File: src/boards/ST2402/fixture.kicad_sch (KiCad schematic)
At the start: 24 parts, among them J11 Conn_02x02_Top_Bottom, J12 Conn_02x02_Top_Bottom, J13 BNC, J14 Screw_Terminal_01x01, J18 Screw_Terminal_01x01, J19 BNC, J21 Conn_02x03_Top_Bottom, J22 Conn_02x03_Top_Bottom

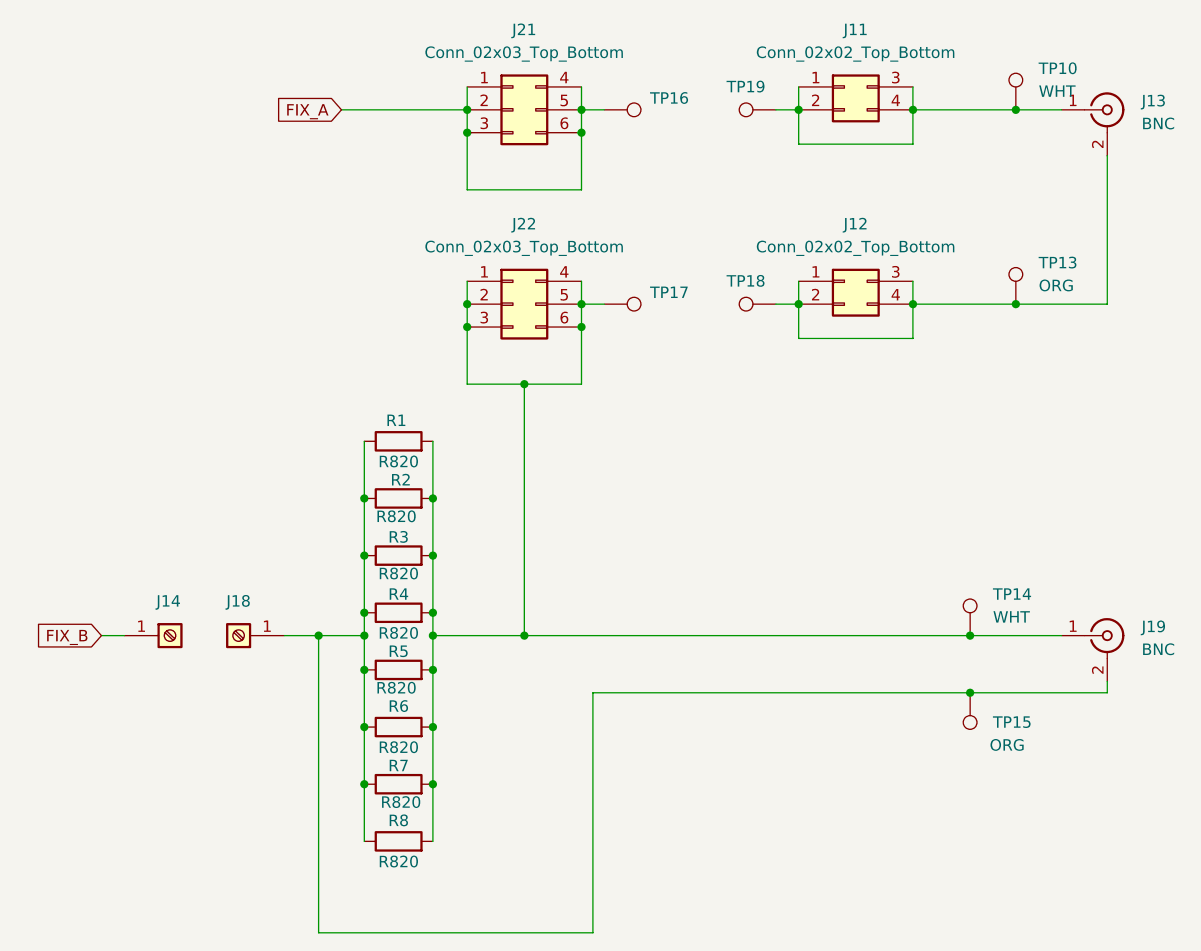
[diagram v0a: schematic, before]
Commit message: Updated pcb files
Added r2 and r3 gerbers and updated KiCad file (r3)
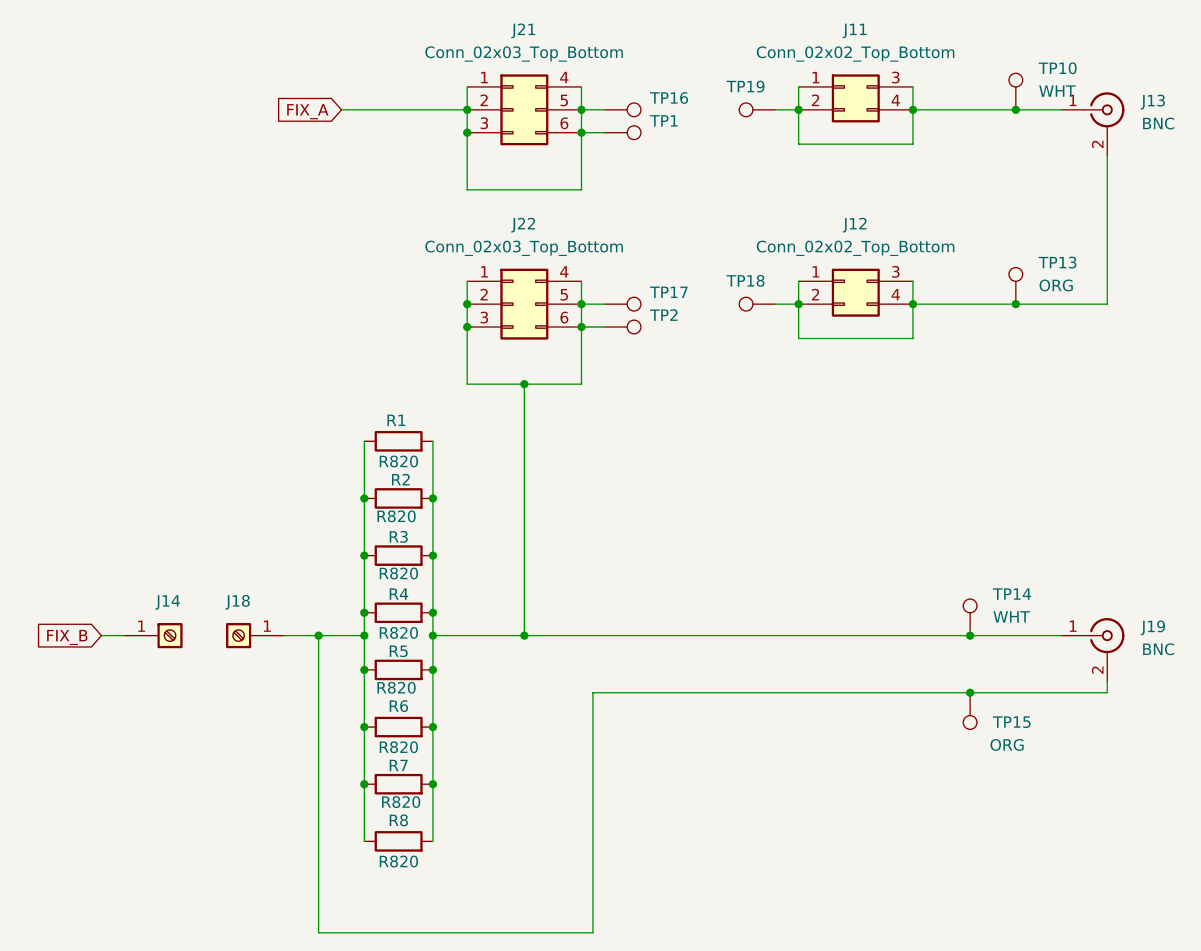
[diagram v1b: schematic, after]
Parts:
- added TP1, TP2: TestPoint, TestPoint:TestPoint_Plated_Hole_D5.0mm, symbol Connector:TestPoint
- J13, J19: footprint Connector_Coaxial:BNC_Amphenol_B6252HB-NPP3G-50_Horizontal -> Connector_Coaxial:BNC_TEConnectivity_1478204_Vertical
- R1, R2, R3, R4, R5, R6, R7, R8: footprint Resistor_SMD:R_0805_2012Metric -> Resistor_SMD:R_1206_3216Metric
- TP10, TP13, TP14, TP15: footprint TestPoint:TestPoint_THTPad_D2.0mm_Drill1.0mm -> TestPoint:TestPoint_Keystone_5010-5014_Multipurpose
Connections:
- net FIX_A: now also TP1.1
- net at J19.1 (In), J22.1 (Pin_1), J22.2 (Pin_2)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: now also TP2.1
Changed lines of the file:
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@@
 (kicad_sch
-	(version 20231120)
+	(version 20250114)
 	(generator "eeschema")
-	(generator_version "8.0")
+	(generator_version "9.0")
 	(paper "USLetter")
 	(title_block
@@
 	(wire
 		(pts
+			(xy 124.46 58.42) (xy 127 58.42)
+		)
+		(stroke
+			(width 0)
+			(type default)
+		)
+	)
+	(wire
+		(pts
 			(xy 161.29 55.88) (xy 161.29 59.69)
 		)
@@
 		(pts
 			(xy 161.29 53.34) (xy 161.29 55.88)
+		)
+		(stroke
+			(width 0)
+			(type default)
+		)
+	)
+	(wire
+		(pts
+			(xy 124.46 80.01) (xy 127 80.01)
 		)
 		(stroke
@@
 			)
 		)
-		(property "Footprint" "TestPoint:TestPoint_THTPad_D2.0mm_Drill1.0mm"
+		(property "Footprint" "TestPoint:TestPoint_Keystone_5010-5014_Multipurpose"
 			(at 177.8 55.88 0)
 			(effects
@@
 			)
 		)
-		(property "Footprint" "Resistor_SMD:R_0805_2012Metric"
+		(property "Footprint" "Resistor_SMD:R_1206_3216Metric"
 			(at 104.14 113.538 90)
 			(effects
@@
 			)
 		)
-		(property "Footprint" "Resistor_SMD:R_0805_2012Metric"
+		(property "Footprint" "Resistor_SMD:R_1206_3216Metric"
 			(at 104.14 126.238 90)
 			(effects
@@
 			)
 		)
-		(property "Footprint" "TestPoint:TestPoint_THTPad_D2.0mm_Drill1.0mm"
+		(property "Footprint" "TestPoint:TestPoint_Keystone_5010-5014_Multipurpose"
 			(at 172.72 114.3 0)
 			(effects
@@
 			)
 		)
-		(property "Footprint" "Connector_Coaxial:BNC_Amphenol_B6252HB-NPP3G-50_Horizontal"
+		(property "Footprint" "Connector_Coaxial:BNC_TEConnectivity_1478204_Vertical"
 			(at 182.88 55.88 0)
 			(effects
@@
 			)
 		)
-		(property "Footprint" "Resistor_SMD:R_0805_2012Metric"
+		(property "Footprint" "Resistor_SMD:R_1206_3216Metric"
 			(at 104.14 94.488 90)
 			(effects
@@
 				(path "/05d99ba5-bbac-4bd6-931a-0f6166a2e0ac/5d4490ae-cd76-4641-b1a2-87213113c349"
 					(reference "R1")
+					(unit 1)
+				)
+			)
+		)
+	)
+	(symbol
+		(lib_id "Connector:TestPoint")
+		(at 127 58.42 270)
+		(unit 1)
+		(exclude_from_sim no)
+		(in_bom yes)
+		(on_board yes)
+		(dnp no)
+		(fields_autoplaced yes)
+		(property "Reference" "TP1"
+			(at 132.08 57.1499 90)
+			(effects
+				(font
+					(size 1.27 1.27)
+				)
+				(justify left)
+			)
+		)
+		(property "Value" "TestPoint"
+			(at 132.08 59.6899 90)
+			(effects
+				(font
+					(size 1.27 1.27)
+				)
+				(justify left)
+				(hide yes)
+			)
+		)
+		(property "Footprint" "TestPoint:TestPoint_Plated_Hole_D5.0mm"
+			(at 127 63.5 0)
+			(effects
+				(font
+					(size 1.27 1.27)
+				)
+				(hide yes)
+			)
+		)
+		(property "Datasheet" "~"
+			(at 127 63.5 0)
+			(effects
+				(font
+					(size 1.27 1.27)
+				)
+				(hide yes)
+			)
+		)
+		(property "Description" "test point"
+			(at 127 58.42 0)
+			(effects
+				(font
+					(size 1.27 1.27)
+				)
+				(hide yes)
+			)
+		)
+		(pin "1"
+		)
+		(instances
+			(project "ST2402"
+				(path "/05d99ba5-bbac-4bd6-931a-0f6166a2e0ac/5d4490ae-cd76-4641-b1a2-87213113c349"
+					(reference "TP1")
+					(unit 1)
+				)
+			)
+		)
+	)
+	(symbol
+		(lib_id "Connector:TestPoint")
+		(at 127 80.01 270)
+		(unit 1)
+		(exclude_from_sim no)
+		(in_bom yes)
+		(on_board yes)
+		(dnp no)
+		(fields_autoplaced yes)
+		(property "Reference" "TP2"
+			(at 132.08 78.7399 90)
+			(effects
+				(font
+					(size 1.27 1.27)
+				)
+				(justify left)
+			)
+		)
+		(property "Value" "TestPoint"
+			(at 132.08 81.2799 90)
+			(effects
+				(font
+					(size 1.27 1.27)
+				)
+				(justify left)
+				(hide yes)
+			)
+		)
+		(property "Footprint" "TestPoint:TestPoint_Plated_Hole_D5.0mm"
+			(at 127 85.09 0)
+			(effects
+				(font
+					(size 1.27 1.27)
+				)
+				(hide yes)
+			)
+		)
+		(property "Datasheet" "~"
+			(at 127 85.09 0)
+			(effects
+				(font
+					(size 1.27 1.27)
+				)
+				(hide yes)
+			)
+		)
+		(property "Description" "test point"
+			(at 127 80.01 0)
+			(effects
+				(font
+					(size 1.27 1.27)
+				)
+				(hide yes)
+			)
+		)
+		(pin "1"
+		)
+		(instances
+			(project "ST2402"
+				(path "/05d99ba5-bbac-4bd6-931a-0f6166a2e0ac/5d4490ae-cd76-4641-b1a2-87213113c349"
+					(reference "TP2")
 					(unit 1)
 				)
@@
 			)
 		)
-		(property "Footprint" "Resistor_SMD:R_0805_2012Metric"
+		(property "Footprint" "Resistor_SMD:R_1206_3216Metric"
 			(at 104.14 119.888 90)
 			(effects
@@
 			)
 		)
-		(property "Footprint" "Resistor_SMD:R_0805_2012Metric"
+		(property "Footprint" "Resistor_SMD:R_1206_3216Metric"
 			(at 104.14 100.838 90)
 			(effects
@@
 			)
 		)
-		(property "Footprint" "Resistor_SMD:R_0805_2012Metric"
+		(property "Footprint" "Resistor_SMD:R_1206_3216Metric"
 			(at 104.14 132.588 90)
 			(effects
@@
 			)
 		)
-		(property "Footprint" "Connector_Coaxial:BNC_Amphenol_B6252HB-NPP3G-50_Horizontal"
+		(property "Footprint" "Connector_Coaxial:BNC_TEConnectivity_1478204_Vertical"
 			(at 182.88 114.3 0)
 			(effects
@@
 			)
 		)
-		(property "Footprint" "TestPoint:TestPoint_THTPad_D2.0mm_Drill1.0mm"
+		(property "Footprint" "TestPoint:TestPoint_Keystone_5010-5014_Multipurpose"
 			(at 162.56 120.65 0)
 			(effects
@@
 			)
 		)
-		(property "Footprint" "Resistor_SMD:R_0805_2012Metric"
+		(property "Footprint" "Resistor_SMD:R_1206_3216Metric"
 			(at 104.14 107.188 90)
 			(effects
@@
 			)
 		)
-		(property "Footprint" "TestPoint:TestPoint_THTPad_D2.0mm_Drill1.0mm"
+		(property "Footprint" "TestPoint:TestPoint_Keystone_5010-5014_Multipurpose"
 			(at 177.8 77.47 0)
 			(effects
@@
 			)
 		)
-		(property "Footprint" "Resistor_SMD:R_0805_2012Metric"
+		(property "Footprint" "Resistor_SMD:R_1206_3216Metric"
 			(at 104.14 138.938 90)
 			(effects
